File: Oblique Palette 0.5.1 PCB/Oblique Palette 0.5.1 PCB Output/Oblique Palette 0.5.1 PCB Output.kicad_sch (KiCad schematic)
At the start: 19 parts, among them J39 Conn_01x02_Pin, J40 Conn_01x03_Female_Pin, J42 AudioJack2_SwitchT, U11 MCP4725xxx-xCH, U12 MCP6004

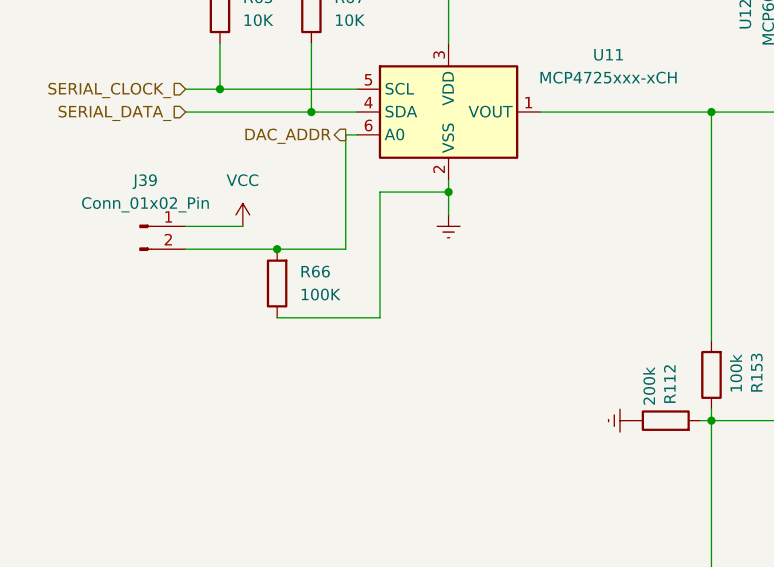
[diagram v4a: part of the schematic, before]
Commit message: All traces(?) now connected on PCB.
This is looking good to me. Vcc and VServo are merged for simplicity. Not the best solution. I think maybe a breakable trace or a single jumper might be the way to do this.
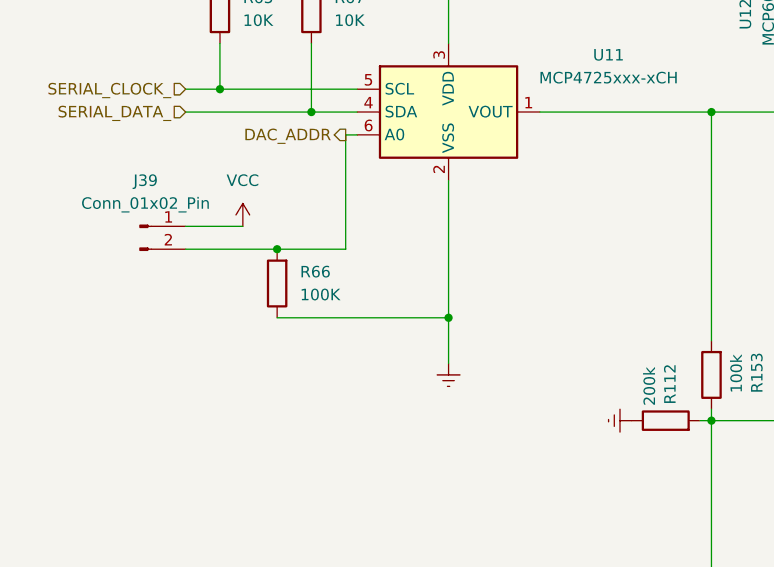
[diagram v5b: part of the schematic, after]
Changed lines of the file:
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@@
 	)
 	(junction
-		(at 73.66 53.34)
+		(at 73.66 67.31)
 		(diameter 0)
 		(color 0 0 0 0)
@@
 	(wire
 		(pts
-			(xy 66.04 67.31) (xy 54.61 67.31)
+			(xy 54.61 67.31) (xy 73.66 67.31)
 		)
 		(stroke
@@
 	(wire
 		(pts
-			(xy 66.04 53.34) (xy 66.04 67.31)
-		)
-		(stroke
-			(width 0)
-			(type default)
-		)
-	)
-	(wire
-		(pts
 			(xy 102.87 113.03) (xy 115.57 113.03)
 		)
@@
 	(wire
 		(pts
+			(xy 73.66 52.07) (xy 73.66 67.31)
+		)
+		(stroke
+			(width 0)
+			(type default)
+		)
+	)
+	(wire
+		(pts
 			(xy 111.76 134.62) (xy 111.76 152.4)
 		)
@@
 	(wire
 		(pts
-			(xy 73.66 52.07) (xy 73.66 53.34)
-		)
-		(stroke
-			(width 0)
-			(type default)
-		)
-	)
-	(wire
-		(pts
 			(xy 115.57 54.61) (xy 115.57 49.53)
 		)
@@
 	(wire
 		(pts
+			(xy 73.66 67.31) (xy 73.66 72.39)
+		)
+		(stroke
+			(width 0)
+			(type default)
+		)
+	)
+	(wire
+		(pts
 			(xy 212.09 49.53) (xy 219.71 49.53)
 		)
@@
 	(wire
 		(pts
-			(xy 73.66 53.34) (xy 73.66 55.88)
-		)
-		(stroke
-			(width 0)
-			(type default)
-		)
-	)
-	(wire
-		(pts
 			(xy 102.87 69.85) (xy 102.87 44.45)
 		)
@@
 		(pts
 			(xy 58.42 44.45) (xy 63.5 44.45)
-		)
-		(stroke
-			(width 0)
-			(type default)
-		)
-	)
-	(wire
-		(pts
-			(xy 73.66 53.34) (xy 66.04 53.34)
 		)
 		(stroke
@@
 	(symbol
 		(lib_id "power:GNDREF")
-		(at 73.66 55.88 0)
+		(at 73.66 72.39 0)
 		(unit 1)
 		(exclude_from_sim no)
@@
 		(fields_autoplaced yes)
 		(property "Reference" "#PWR0205"
-			(at 73.66 62.23 0)
+			(at 73.66 78.74 0)
 			(effects
 				(font
@@
 		)
 		(property "Value" "GNDREF"
-			(at 73.66 60.96 0)
+			(at 73.66 77.47 0)
 			(effects
 				(font
@@
 		)
 		(property "Footprint" ""
-			(at 73.66 55.88 0)
+			(at 73.66 72.39 0)
 			(effects
 				(font
@@
 		)
 		(property "Datasheet" ""
-			(at 73.66 55.88 0)
+			(at 73.66 72.39 0)
 			(effects
 				(font
@@
 		)
 		(property "Description" "Power symbol creates a global label with name \"GNDREF\" , reference supply ground"
-			(at 73.66 55.88 0)
-			(effects
-				(font
+			(at 73.66 72.39 0)
+			(effects
+				(font

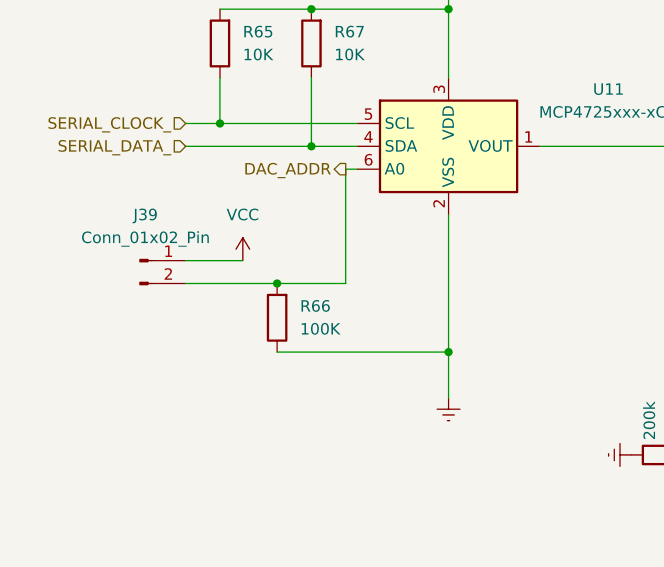
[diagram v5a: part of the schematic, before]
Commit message: All traces connected. Replaced caps with 1mF SMD ones to add muffling power for and to the servos.
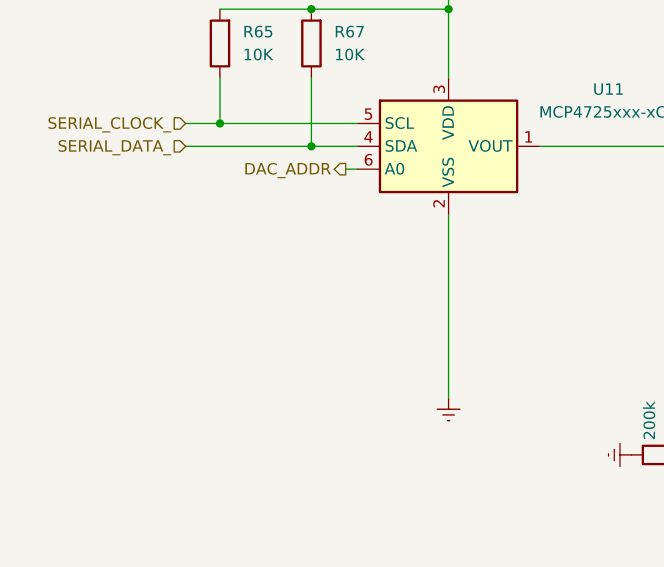
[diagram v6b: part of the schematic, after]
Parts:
- removed J39: Conn_01x02_Pin, Connector_PinHeader_2.54mm:PinHeader_1x02_P2.54mm_Vertical, symbol Connector:Conn_01x02_Pin
- removed R66: 100K, Resistor_SMD:R_0805_2012Metric, symbol Device:R
